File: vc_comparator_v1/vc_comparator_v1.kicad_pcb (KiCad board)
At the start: 2 copper layers, 28 x 100 mm, 67 parts, among them J1 Conn_02x05_Odd_Even, J2 SIGNAL, J3 OUT, J4 LEVEL, J5 OUT_INV, U1 LM393, U2 LM358, U3 LM358, U4 LM358

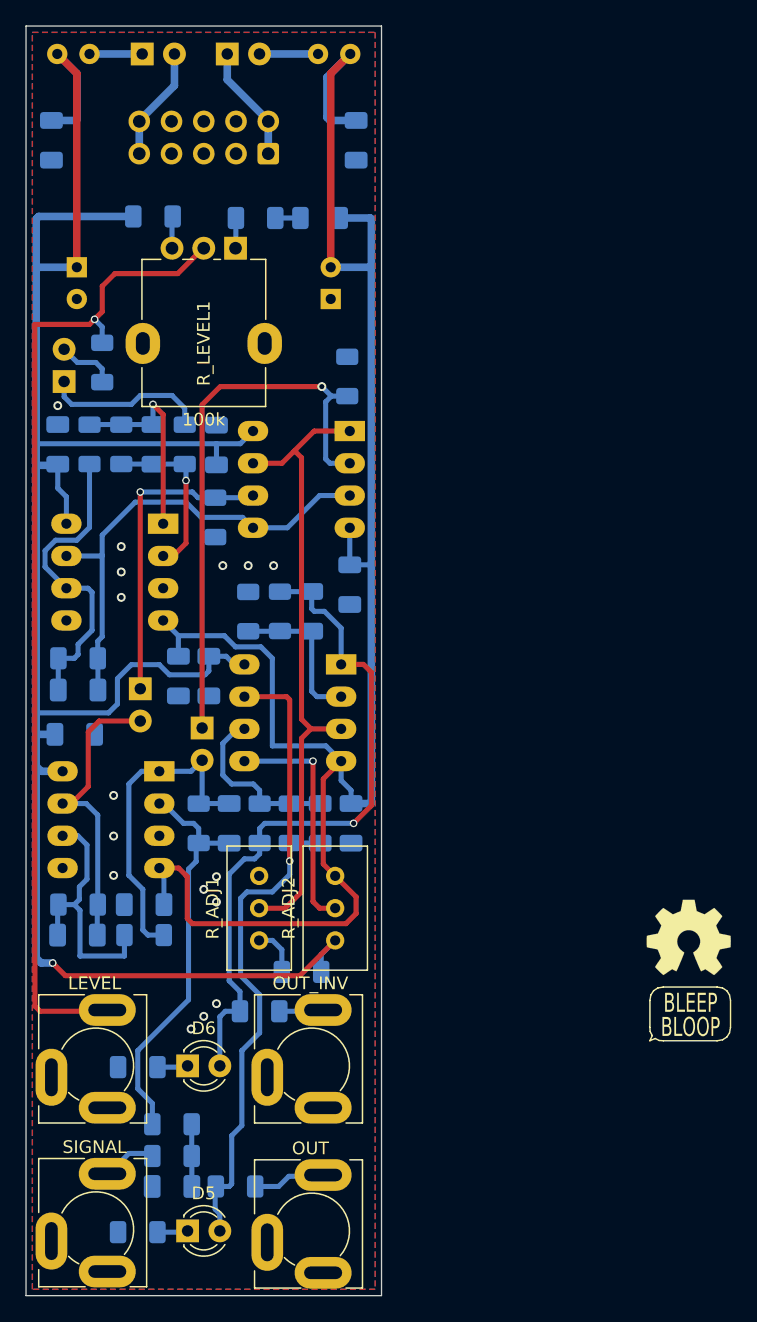
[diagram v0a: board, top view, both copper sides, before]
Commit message: Geographic re-annotate and cleanup
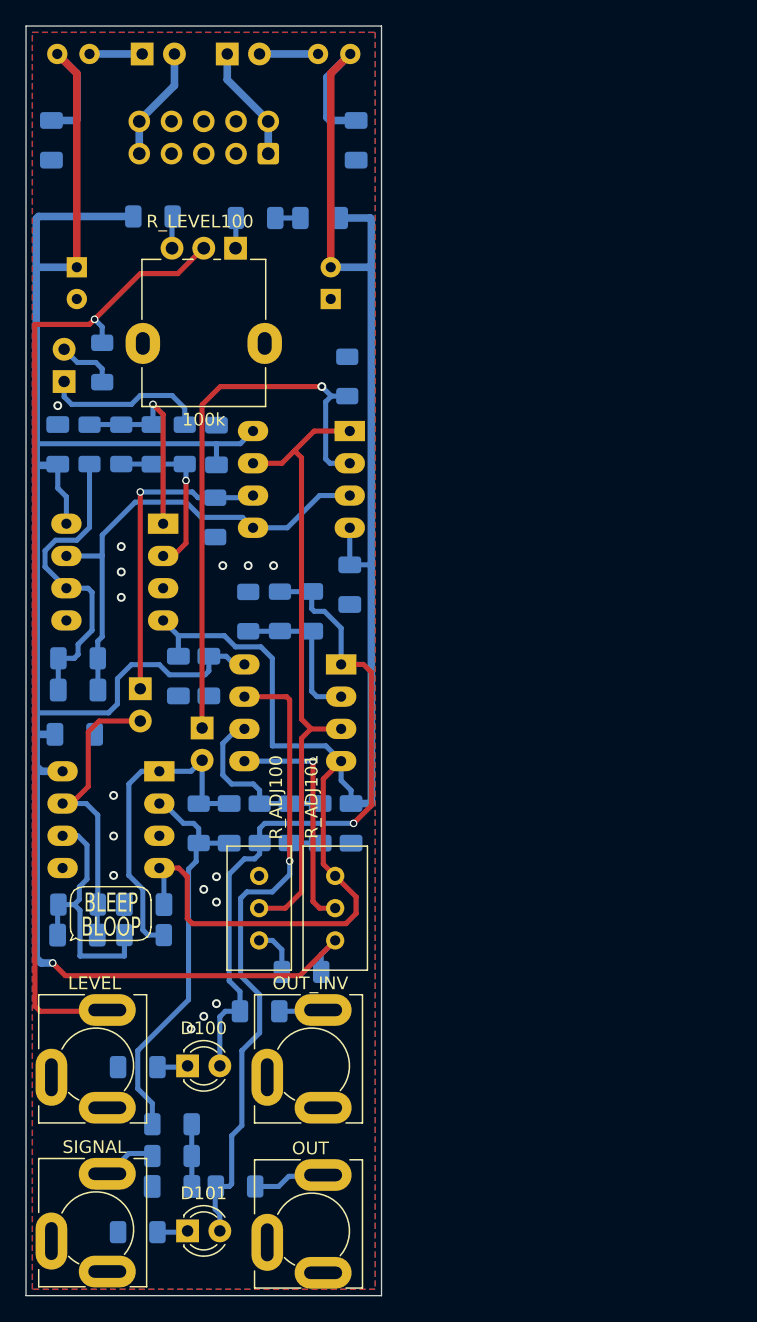
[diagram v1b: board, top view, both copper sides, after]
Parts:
- LOGO100: renamed from LOGO3; moved to B.Cu
- moved LOGO102 64.6 mm to (154.0, 75.8)
- moved LOGO101 46.3 mm to (146.7, 119.9)
- moved LOGO100 37.6 mm to (154.7, 123.2), turned to 180 degrees
- renumbered C8 to C1, C5 to C10, C12 to C11, C18 to C12, C4 to C13, C11 to C14, C16 to C15, C15 to C16, C10 to C17, C14 to C18, C13 to C19, C1 to C3, C7 to C4, C3 to C5, C19 to C6, C6 to C7, C9 to C8, C17 to C9, D6 to D100, D5 to D101, D1 to D2, D2 to D3, D7 to D4, D3 to D5, D4 to D6, J4 to J100, J5 to J101, J2 to J102, J3 to J103, J1 to J2, LOGO1 to LOGO101, LOGO2 to LOGO102, R16 to R1, R13 to R10, R19 to R11, R22 to R12, R11 to R13, R9 to R14, R6 to R15, R4 to R16, R1 to R17, R5 to R18, R17 to R19, R15 to R2, R24 to R20, R3 to R21, R2 to R22, R12 to R23, R7 to R24, R14 to R3, R20 to R4, R8 to R5, R21 to R6, R23 to R7, R18 to R8, R10 to R9, R_ADJ1 to R_ADJ100, R_ADJ2 to R_ADJ101, R_LEVEL1 to R_LEVEL100, U4 to U2, U2 to U4
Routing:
- net Net-(J100-PadT): track 78.6 -> 77.4 mm
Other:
- board text added: "LM358"
- board text added: "LM393"
- board text added: "VC Comparator"
- board text added: "v1.0 Oct 2022"
- board text removed: "Eurorack Template"
- board text removed: "v1.1 July 2022"
